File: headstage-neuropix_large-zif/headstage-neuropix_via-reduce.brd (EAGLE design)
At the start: 21.2 x 51.5 mm, 147 parts, among them J1 302-S101, J2 X.FL-R-SMT-1(02), J3 FH23-45S-0.3SHW(05), J4 77311-118-02LF, J5 FH23-45S-0.3SHW(05), U1 10M08SAM15317G, U10 BNO055, U11 DSC6102MI2A-093.6000, U12 PL133-27GC-R, U13 TS4231, U14 TS4231, U15 TS4231, U2 ASCO2-24.000MHZ-EK-T3, U3 MAX4945AELA+T, U4 ADP7112ACBZ-1.8-R7, U5 DS90UB933_WQFN, U6 NCP161BMX330, U7 TPS8268180, U8 TLV70712, U9 ADP7112ACBZ-1.2-R7, X2 OE-LOGO_14X10

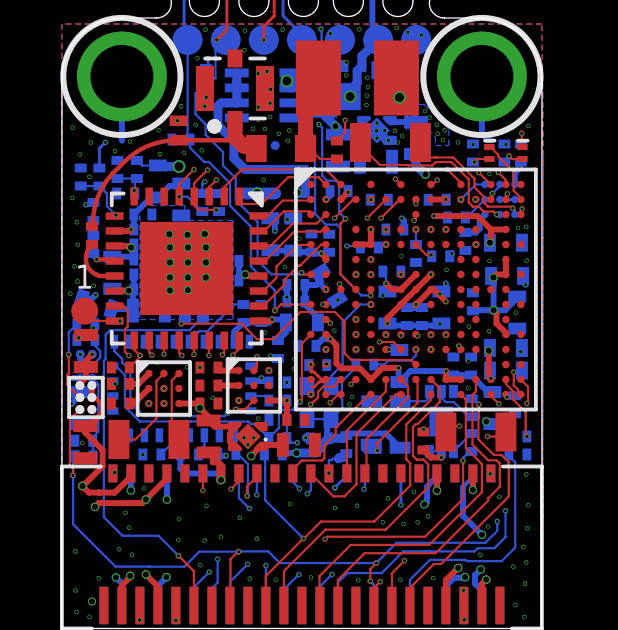
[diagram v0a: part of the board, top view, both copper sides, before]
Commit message: Correct tPlace/tStop mixup for ADP7112's
- Solder pads had tPlace instead of tStop so there would have been
silkscreen on the pads
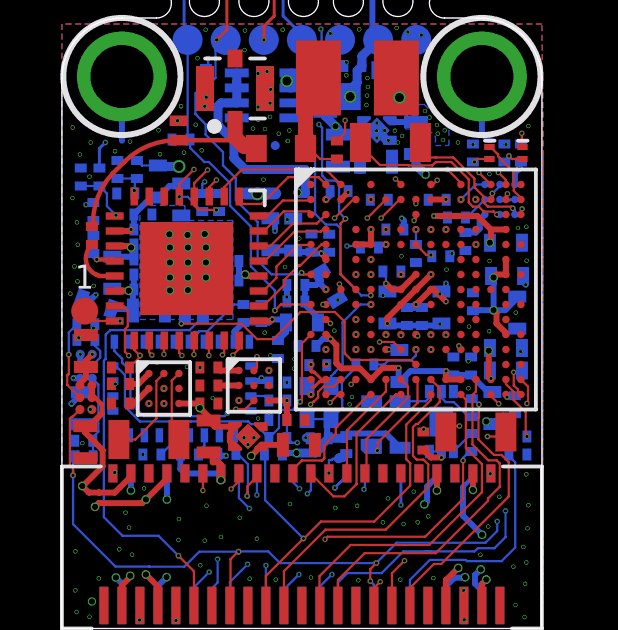
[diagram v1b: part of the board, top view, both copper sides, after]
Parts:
- U10: device jonnew:LGA-28-3.8X5.2 -> jonnew:LGA-28-3.8X2.5-LP
- U4, U9: device jonnew:WLCSP6-1X1.2 -> jonnew:WLCSP6-1X1.2-LP
- U5: device jonnew:WQFN32-5X5 -> jonnew:WQFN32-5X5-LP
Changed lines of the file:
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@@
 <setting verticaltext="up"/>
 </settings>
-<grid distance="1" unitdist="mil" unit="mil" style="lines" multiple="1" display="yes" altdistance="5" altunitdist="mil" altunit="mil"/>
+<grid distance="0.1" unitdist="mm" unit="mm" style="lines" multiple="1" display="yes" altdistance="5" altunitdist="mil" altunit="mil"/>
 <layers>
 <layer number="1" name="Highspeed1" color="4" fill="1" visible="yes" active="yes"/>
@@
 <element name="U6" library="jonnew" package="X2SON" value="NCP161BMX330" x="2.5" y="15.6" smashed="yes" rot="MR0"/>
 <element name="U8" library="jonnew" package="X2SON" value="TLV70712" x="-1.8" y="5.4" smashed="yes" rot="R180"/>
-<element name="U5" library="jonnew" package="WQFN32-5X5" value="DS90UB933_WQFN" x="-3.84" y="11" smashed="yes"/>
+<element name="U5" library="jonnew" package="WQFN32-5X5-LP" value="DS90UB933_WQFN" x="-3.84" y="11" smashed="yes"/>
 <element name="J2" library="jonnew" package="X_FL_R_SMT_1(02)" value="X.FL-R-SMT-1(02)" x="-2.23" y="17" smashed="yes"/>
 <element name="D3" library="jonnew" package="0402T-DFN" value="SESD0402X1UN-0020-090" x="-4.11" y="15.6" smashed="yes" rot="R270"/>
@@
 <element name="C29" library="jonnew" package="0201T" value="0.1uF" x="-1.95" y="9.5" smashed="yes" rot="MR90"/>
 <element name="C27" library="jonnew" package="0201T" value="0.1uF" x="-0.8" y="7.2" smashed="yes" rot="MR180"/>
-<element name="U10" library="jonnew" package="LGA-28-3.8X5.2" value="BNO055" x="-4" y="7" smashed="yes" rot="MR0"/>
+<element name="U10" library="jonnew" package="LGA-28-3.8X2.5-LP" value="BNO055" x="-4" y="7" smashed="yes" rot="MR0"/>
 <element name="C39" library="jonnew" package="0201T" value="0.1uF" x="-3.75" y="4.8" smashed="yes" rot="MR180"/>
 <element name="R20" library="jonnew" package="0201T" value="10k" x="-5" y="4.8" smashed="yes" rot="MR0"/>
@@
 <element name="C28" library="jonnew" package="0402TW" value="10uF" x="0.78" y="16.76" smashed="yes" rot="MR90"/>
 <element name="C25" library="jonnew" package="0201T" value="1uF" x="1.7" y="17.75" smashed="yes" rot="MR0"/>
-<element name="U4" library="jonnew" package="WLCSP6-1X1.2" value="ADP7112ACBZ-1.8-R7" x="-7.2" y="6.7" smashed="yes"/>
-<element name="U9" library="jonnew" package="WLCSP6-1X1.2" value="ADP7112ACBZ-1.2-R7" x="-7.19" y="7.74" smashed="yes" rot="MR0"/>
+<element name="U4" library="jonnew" package="WLCSP6-1X1.2-LP" value="ADP7112ACBZ-1.8-R7" x="-7.2" y="6.7" smashed="yes"/>
+<element name="U9" library="jonnew" package="WLCSP6-1X1.2-LP" value="ADP7112ACBZ-1.2-R7" x="-7.19" y="7.74" smashed="yes" rot="MR0"/>
 <element name="C30" library="jonnew" package="0201T" value="1nF" x="-7.2" y="9.14" smashed="yes" rot="MR180"/>
 <element name="C33" library="jonnew" package="0402TW" value="10uF" x="-7.22" y="5.21" smashed="yes" rot="R270"/>
